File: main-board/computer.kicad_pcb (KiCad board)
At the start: 2 copper layers, 141 x 76.8 mm, 26 parts, among them J1 Conn_02x20_Odd_Even, J2 Conn_02x20_Odd_Even, J3 PORT A, J4 PORT B, J5 SERIAL, SW1 RESET, U1 W65C02S, U11 DS1813, U2 AS6C62256-55, U3 SST39SF010, U4 W65C22N, U5 W65C51N, U6 74HC00, U7 74HC30, U8 74HC138, X1 1.8432MHz

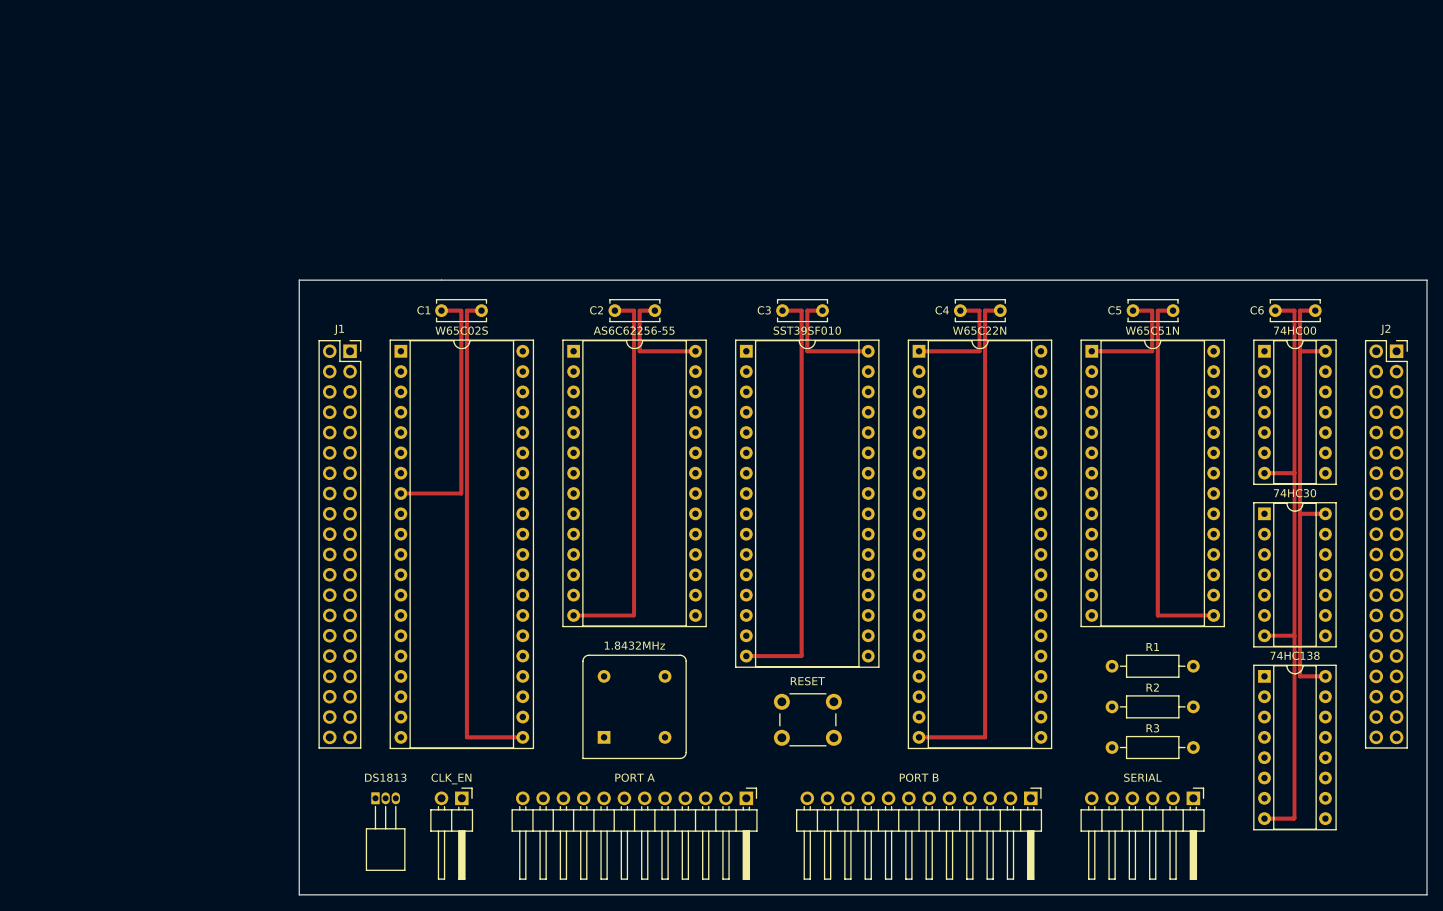
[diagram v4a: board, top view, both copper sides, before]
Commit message: Revert "Integtrate IO into mail board, begion VGA layout"
This reverts commit 15baf3f71fbe492a9e0b6e5b5ec863db56e31855.
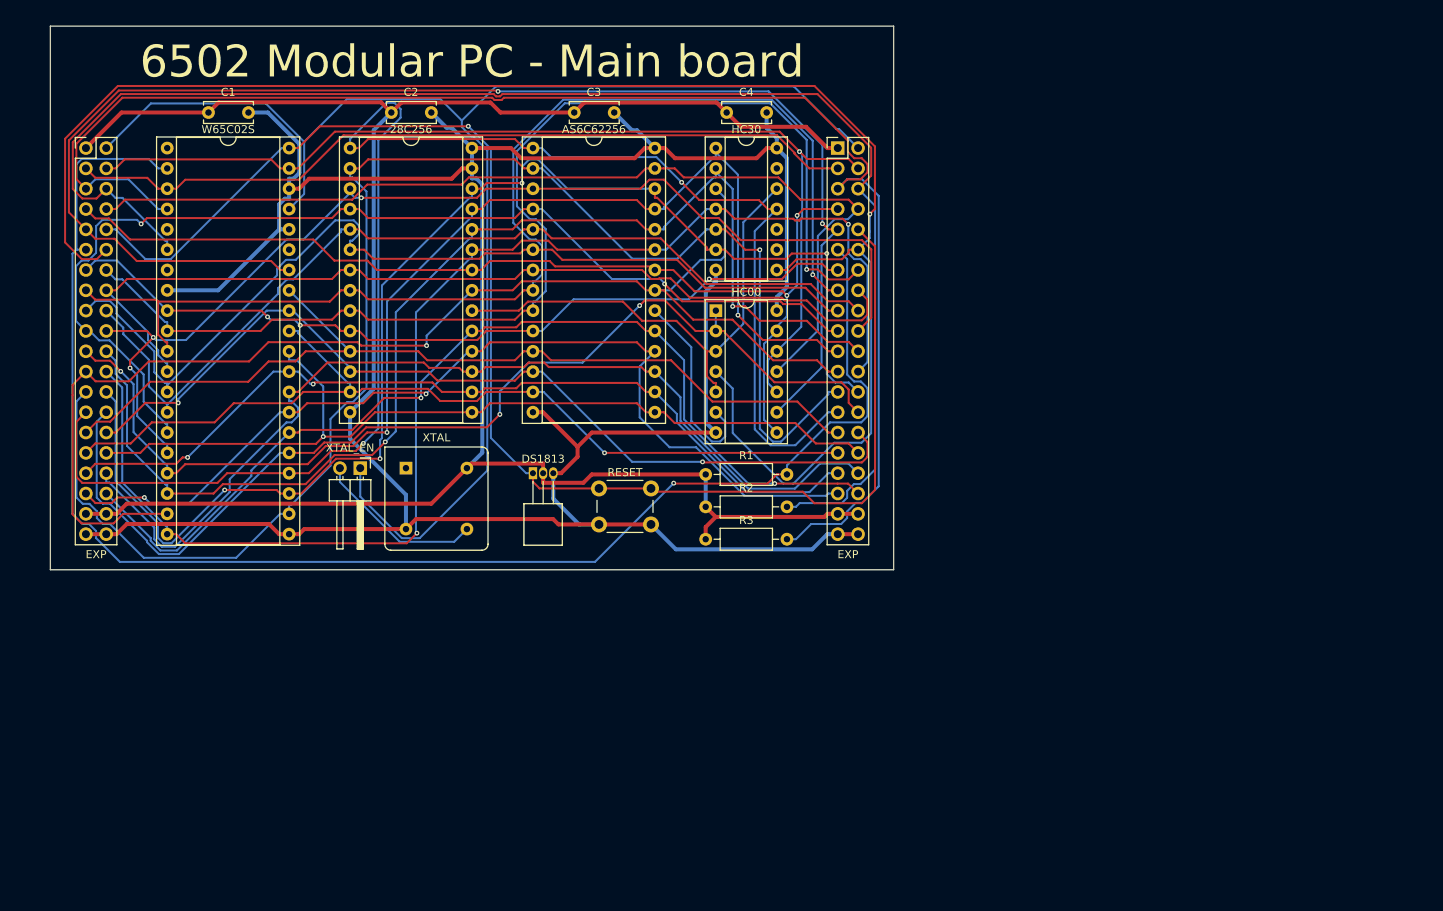
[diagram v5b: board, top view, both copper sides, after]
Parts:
- removed C5, C6: 0.1uF, Capacitor_THT:C_Disc_D6.0mm_W2.5mm_P5.00mm
- removed J1, J2: Conn_02x20_Odd_Even, Connector_PinSocket_2.54mm:PinSocket_2x20_P2.54mm_Vertical
- removed J3: PORT A, Connector_PinHeader_2.54mm:PinHeader_1x12_P2.54mm_Horizontal
- removed J4: PORT B, Connector_PinHeader_2.54mm:PinHeader_1x12_P2.54mm_Horizontal
- removed J5: SERIAL, Connector_PinHeader_2.54mm:PinHeader_1x06_P2.54mm_Horizontal
- removed JP1: CLK_EN, Connector_PinHeader_2.54mm:PinHeader_1x02_P2.54mm_Horizontal
- removed SW1: RESET, Button_Switch_THT:SW_PUSH_6mm
- removed U1: W65C02S, Package_DIP:DIP-40_W15.24mm_Socket
- removed U11: DS1813, Package_TO_SOT_THT:TO-92_Inline_Horizontal1
- removed U2: AS6C62256-55, Package_DIP:DIP-28_W15.24mm_Socket
- removed U3: SST39SF010, Package_DIP:DIP-32_W15.24mm_Socket
- removed U4: W65C22N, Package_DIP:DIP-40_W15.24mm_Socket
- removed U5: W65C51N, Package_DIP:DIP-28_W15.24mm_Socket
- removed U6: 74HC00, Package_DIP:DIP-14_W7.62mm_Socket
- removed U7: 74HC30, Package_DIP:DIP-14_W7.62mm_Socket
- removed U8: 74HC138, Package_DIP:DIP-16_W7.62mm_Socket
- removed X1: 1.8432MHz, Oscillator:Oscillator_DIP-8
- added 28C256: 28C256, Package_DIP:DIP-28_W15.24mm_Socket, F.Cu at (104.1, 34.3)
- added AS6C62256: AS6C62256, Package_DIP:DIP-28_W15.24mm_Socket, F.Cu at (127.0, 34.3)
- added DS1813: DS1813, Package_TO_SOT_THT:TO-92_Inline_Horizontal1, F.Cu at (127.0, 74.9)
- added EXP: Expansion, Connector_PinHeader_2.54mm:PinHeader_2x20_P2.54mm_Vertical, F.Cu at (165.1, 34.3)
- added EXP: Expansion, Connector_PinHeader_2.54mm:PinHeader_2x20_P2.54mm_Vertical, F.Cu at (71.1, 34.3)
- added HC00: 74HC00, Package_DIP:DIP-14_W7.62mm_Socket, F.Cu at (149.9, 54.6)
- added HC30: 74HC30, Package_DIP:DIP-14_W7.62mm_Socket, F.Cu at (149.9, 34.3)
- added RESET: RESET, Button_Switch_THT:SW_PUSH_6mm, F.Cu at (135.3, 76.8)
- added W65C02S: W65C02SxP, Package_DIP:DIP-40_W15.24mm_Socket, F.Cu at (81.3, 34.3)
- added XTAL: 1MHz, Oscillator:Oscillator_DIP-8, F.Cu at (111.1, 74.3)
- added XTAL_EN: Jumper, Connector_PinHeader_2.54mm:PinHeader_1x02_P2.54mm_Horizontal, F.Cu at (105.4, 74.3)
- moved R3 57.1 mm to (148.6, 83.2)
- moved R2 56.6 mm to (148.6, 79.1)
- moved R1 56.2 mm to (148.6, 75.1)
- moved C4 38.3 mm to (156.2, 29.8)
- moved C2 37.3 mm to (114.3, 29.8)
- moved C3 35.9 mm to (137.2, 29.8)
- moved C1 34.6 mm to (91.4, 29.8), turned to 180 degrees
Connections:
- R1 pad 2: !IRQ -> RDY
- R3 pad 2: RDY -> !IRQ
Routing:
- net !P_SELECT: track 0.00 -> 206.4 mm, vias 0 -> 1
- net A14: track 0.00 -> 199.2 mm, vias 0 -> 2
- net RDY: track 0.00 -> 190.7 mm, vias 0 -> 1
- net A12: track 0.00 -> 189.9 mm, vias 0 -> 1
- net !IRQ: track 0.00 -> 187.1 mm
- net CLK: track 0.00 -> 186.0 mm
- net !NMI: track 0.00 -> 183.0 mm
- net !RESET: track 0.00 -> 180.0 mm, vias 0 -> 1
- net R!W: track 0.00 -> 177.2 mm, vias 0 -> 2
- net A11: track 0.00 -> 166.0 mm, vias 0 -> 2
- net A13: track 0.00 -> 165.6 mm, vias 0 -> 4
- net A10: track 0.00 -> 156.1 mm, vias 0 -> 1
- net A8: track 0.00 -> 153.9 mm, vias 0 -> 3
- net A9: track 0.00 -> 153.3 mm, vias 0 -> 2
- net A2: track 0.00 -> 147.7 mm, vias 0 -> 1
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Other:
- board size 141 x 76.8 mm -> 105.4 x 67.9 mm
- board text added: "6502 Modular PC - Main board"
- board text added: "JLCJLCJLCJLC"

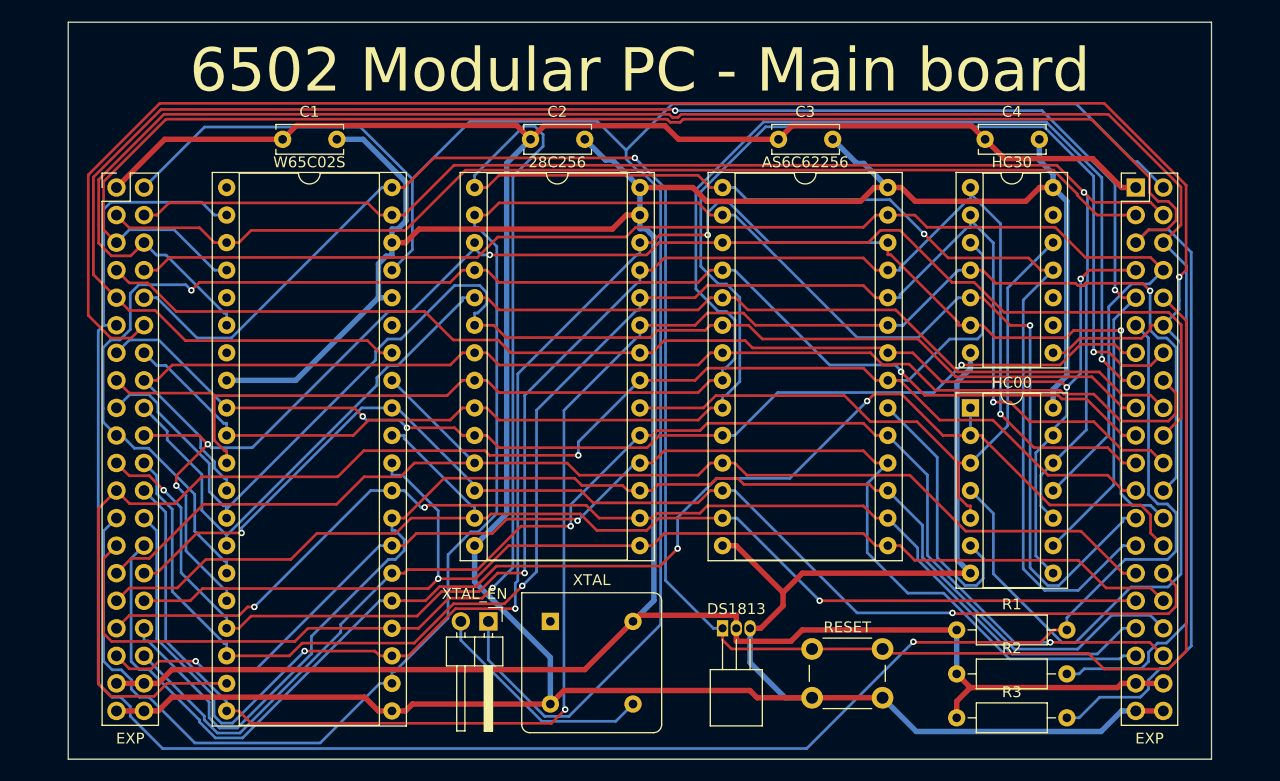
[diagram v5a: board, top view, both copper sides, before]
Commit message: Redesign CPU and IO boards
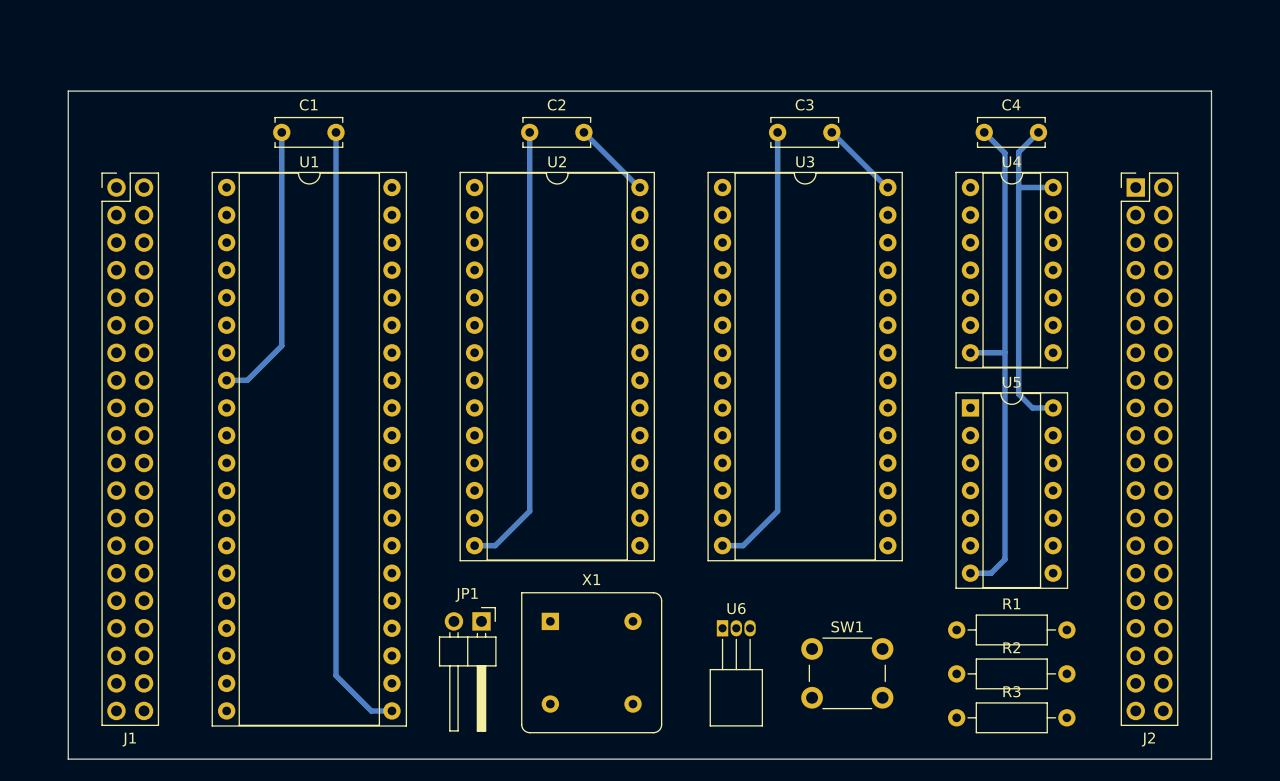
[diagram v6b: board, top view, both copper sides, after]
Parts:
- moved C4 5.12 mm to (151.1, 29.2), turned to 0 degrees
- moved C1 5.12 mm to (86.4, 29.2), turned to 0 degrees
- moved C2 5.12 mm to (109.2, 29.2), turned to 0 degrees
- moved C3 5.12 mm to (132.1, 29.2), turned to 0 degrees
- moved JP1 0.63 mm to (104.8, 74.3)
- renumbered EXP to J1, EXP to J2, XTAL_EN to JP1, RESET to SW1, W65C02S to U1, 28C256 to U2, AS6C62256 to U3, HC30 to U4, HC00 to U5, DS1813 to U6, XTAL to X1
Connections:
- C2 pad 1: +5V -> GND
- C2 pad 2: GND -> +5V
- C3 pad 1: +5V -> GND
- C3 pad 2: GND -> +5V
- C4 pad 1: +5V -> GND
- C4 pad 2: GND -> +5V
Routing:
- net +5V: track 294.7 -> 72.4 mm
- net !P_SELECT: track 206.4 -> 0.00 mm, vias 1 -> 0
- net A14: track 199.2 -> 0.00 mm, vias 2 -> 0
- net RDY: track 190.7 -> 0.00 mm, vias 1 -> 0
- net A12: track 189.9 -> 0.00 mm, vias 1 -> 0
- net !IRQ: track 187.1 -> 0.00 mm
- net CLK: track 186.0 -> 0.00 mm
- net !NMI: track 183.0 -> 0.00 mm
- net !RESET: track 180.0 -> 0.00 mm, vias 1 -> 0
- net R!W: track 177.2 -> 0.00 mm, vias 2 -> 0
- net A11: track 166.0 -> 0.00 mm, vias 2 -> 0
- net A13: track 165.6 -> 0.00 mm, vias 4 -> 0
- net A10: track 156.1 -> 0.00 mm, vias 1 -> 0
- net A8: track 153.9 -> 0.00 mm, vias 3 -> 0
- net A9: track 153.3 -> 0.00 mm, vias 2 -> 0
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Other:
- board size 105.4 x 67.9 mm -> 105.4 x 61.6 mm
- board text removed: "6502 Modular PC - Main board"

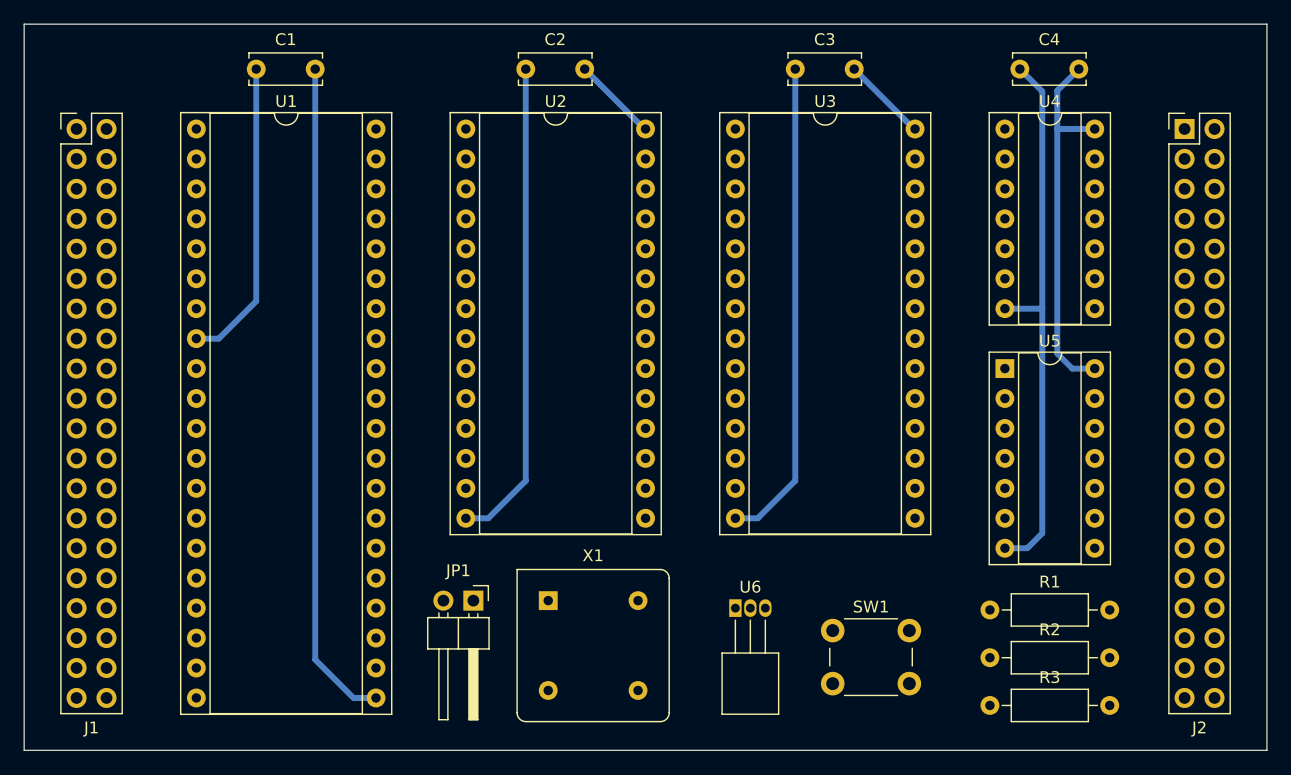
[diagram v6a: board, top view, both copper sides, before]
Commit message: Finish designing and routing new CPU and IO boards
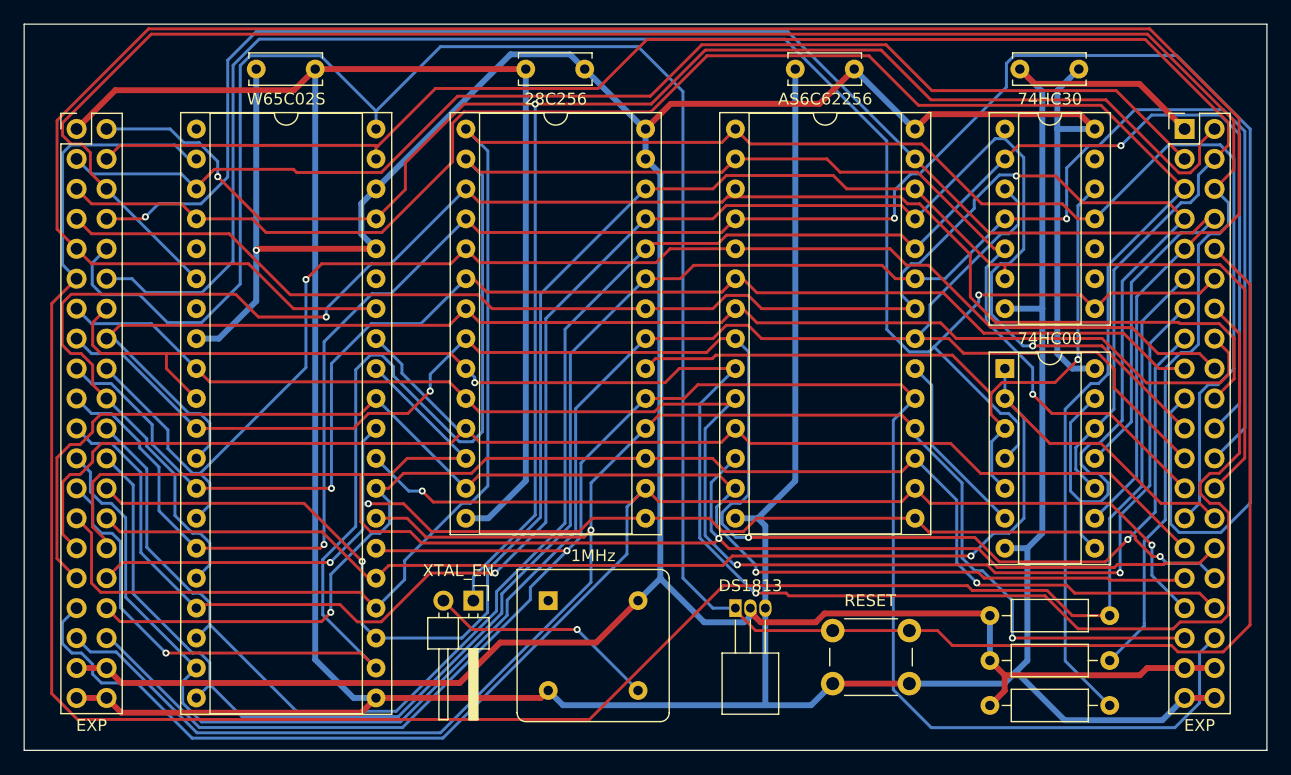
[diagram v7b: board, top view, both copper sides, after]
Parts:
- J1, J2: value Expansion -> EXP
- JP1: value Jumper -> XTAL_EN
- U1: value W65C02SxP -> W65C02S
- moved R1 0.48 mm to (148.6, 75.6)
- moved R2 0.24 mm to (148.6, 79.4)
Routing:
- net +5V: track 72.4 -> 298.3 mm, vias 0 -> 1
- net !RESET: track 0.00 -> 208.7 mm
- net A6: track 0.00 -> 191.7 mm, vias 0 -> 2
- net RDY: track 0.00 -> 186.9 mm
- net R!W: track 0.00 -> 185.7 mm
- net GND: track 186.3 -> 371.5 mm
- net A12: track 0.00 -> 183.8 mm, vias 0 -> 2
- net A14: track 0.00 -> 181.9 mm
- net A11: track 0.00 -> 177.6 mm, vias 0 -> 1
- net !NMI: track 0.00 -> 176.0 mm
- net A9: track 0.00 -> 171.7 mm, vias 0 -> 1
- net D7: track 0.00 -> 164.5 mm, vias 0 -> 1
- net A1: track 0.00 -> 159.9 mm, vias 0 -> 2
- net !IRQ: track 0.00 -> 158.3 mm
- net A13: track 0.00 -> 157.5 mm, vias 0 -> 1
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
